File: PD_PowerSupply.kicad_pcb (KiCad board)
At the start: 4 copper layers, 59.3 x 45.5 mm, 75 parts, among them J1 2.54mm Header, J2 Screw Terminal, Q1 STL6P3LLH6, Q2 STL6P3LLH6, U1 LM1117LD-3.3, U2 STUSB4500QTR, U3 LMR16006YQ5, U4 LTM8074IY, U5 LTC7106EDDB-1, U6 LMP92064SDE_NOPB, U7 AQV252GAX, U8 BMD-340-A-R, U9 USB6B1

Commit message: completed routing. Ready for eval.
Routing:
- net /SCLK: track 2.42 -> 57.0 mm, vias 0 -> 3
- net /LTC7106_EN: track 3.65 -> 57.3 mm, vias 0 -> 2
- net /MISO: track 11.0 -> 64.1 mm, vias 1 -> 3
- net /MOSI: track 7.21 -> 58.3 mm, vias 1 -> 3
- net /LTC7106_CSB: track 2.42 -> 50.8 mm, vias 0 -> 2
- net /LMP92064_CSB: track 2.42 -> 34.8 mm, vias 0 -> 2
- net /STUSB_POK3: track 1.18 -> 26.8 mm, vias 1 -> 2
- net /STUSB_RESET: track 5.18 -> 30.6 mm, vias 0 -> 2
- net /STUSB_POK2: track 9.70 -> 34.6 mm, vias 1 -> 2
- net +5V: track 62.8 -> 80.8 mm, vias 0 -> 2
- net /OUTPUT_EN: track 40.2 -> 56.5 mm, vias 0 -> 2
- net +3V3: track 31.1 -> 33.3 mm, vias 12 -> 14
- net GND: track 104.3 -> 102.8 mm, vias 68 -> 78
- net Net-(R1-Pad2): track 34.1 -> 34.6 mm
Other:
- board size 59.3 x 45.5 mm -> 59.3 x 46 mm

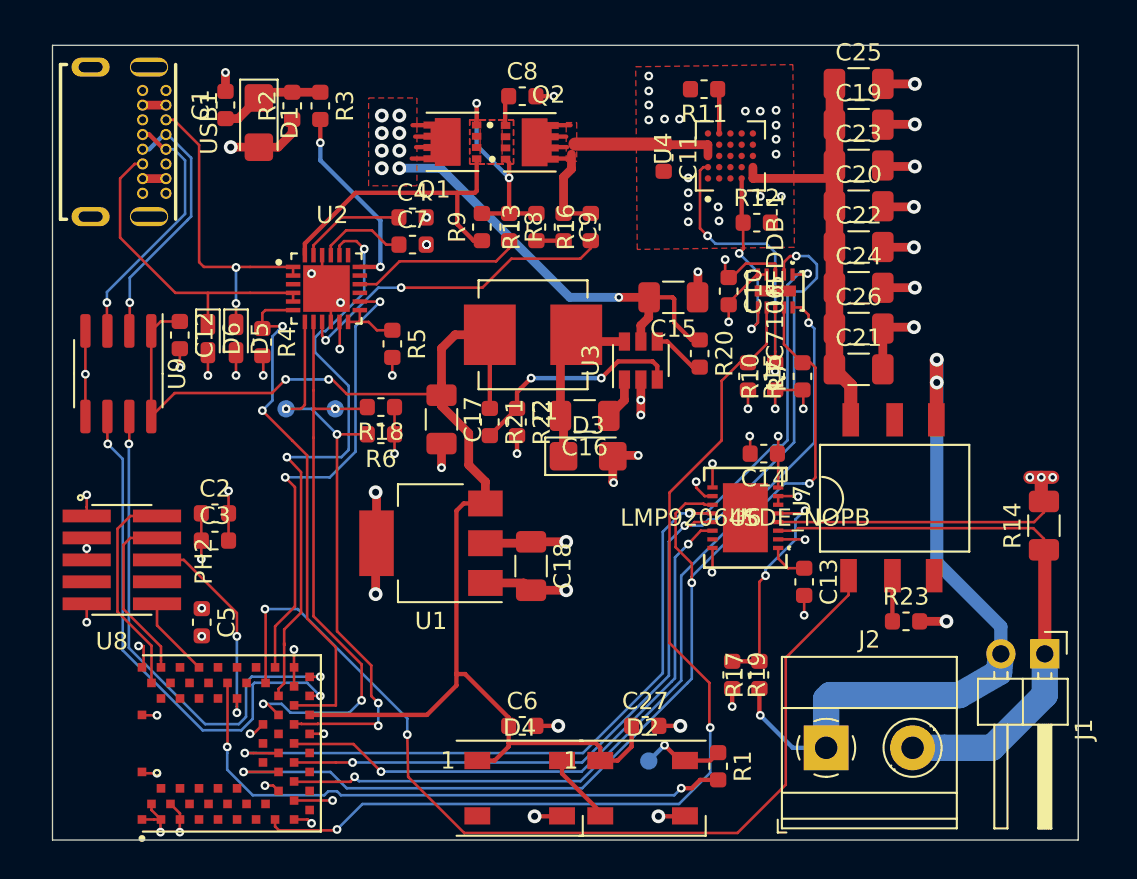
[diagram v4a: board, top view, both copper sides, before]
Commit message: Fixed DRC errors, moved silkscreen
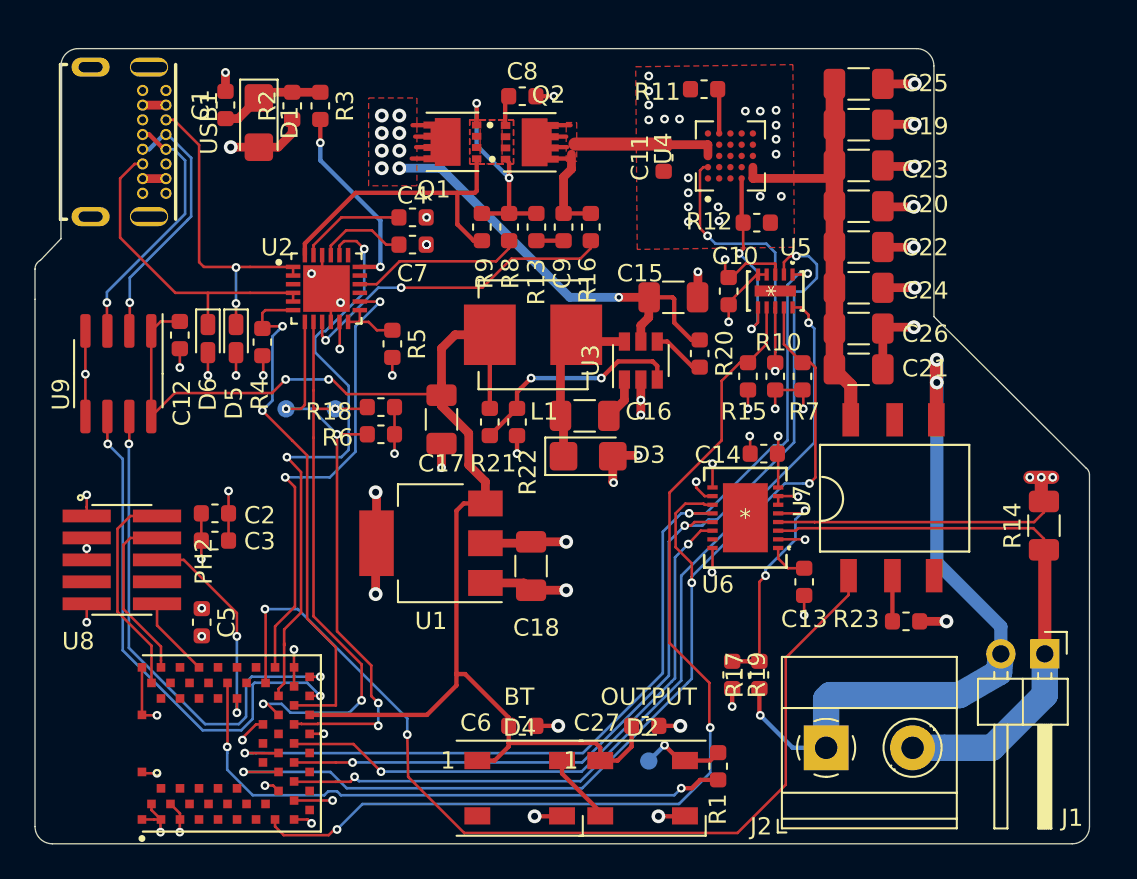
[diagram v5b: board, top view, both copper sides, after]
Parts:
- renumbered TP3 to LED_DATA1
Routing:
- net GND: track 102.8 -> 104.7 mm, vias 78 -> 77
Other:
- board size 59.3 x 46 mm -> 61 x 46 mm
- net class Default: clearance 0.2 -> 0.15
- rule trace_clearance: 0.2 -> 0.15
- board text added: "BT"
- board text added: "OUTPUT"

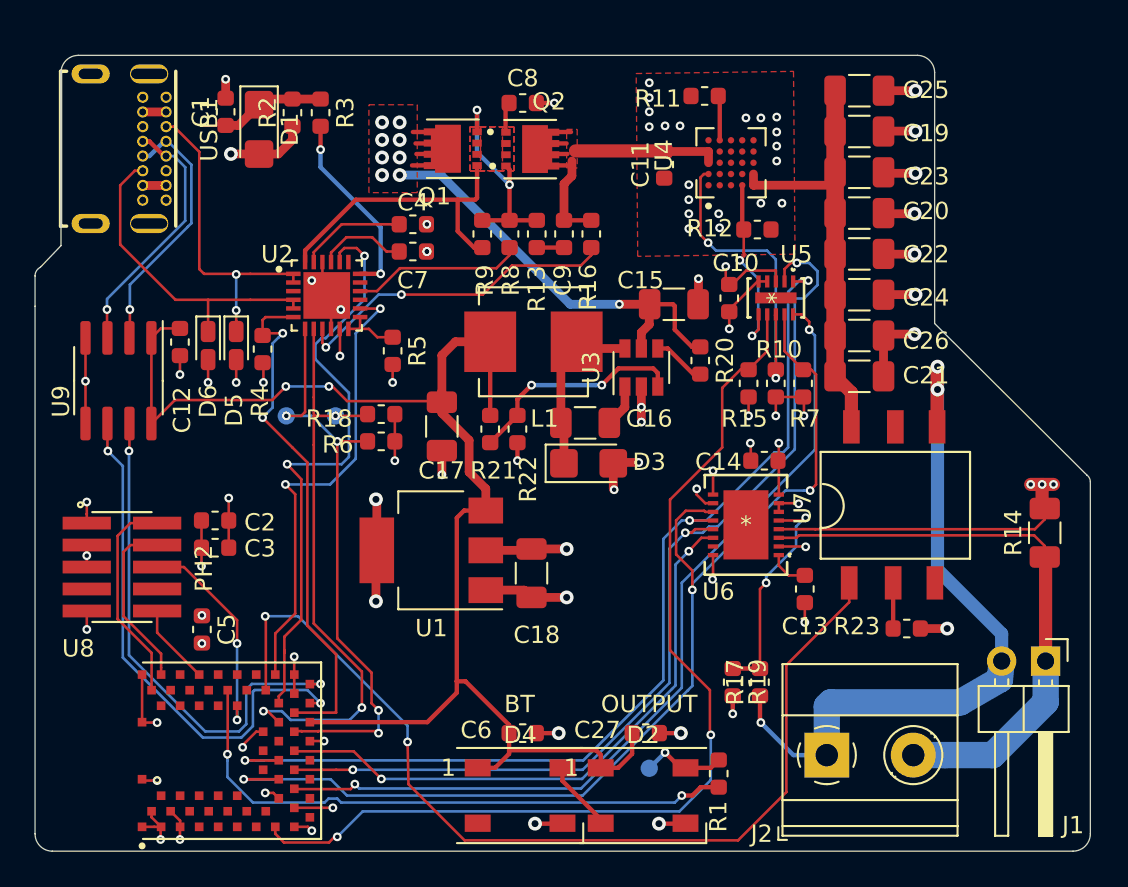
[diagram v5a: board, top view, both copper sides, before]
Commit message: Setup fab drawing and remove designators from silk
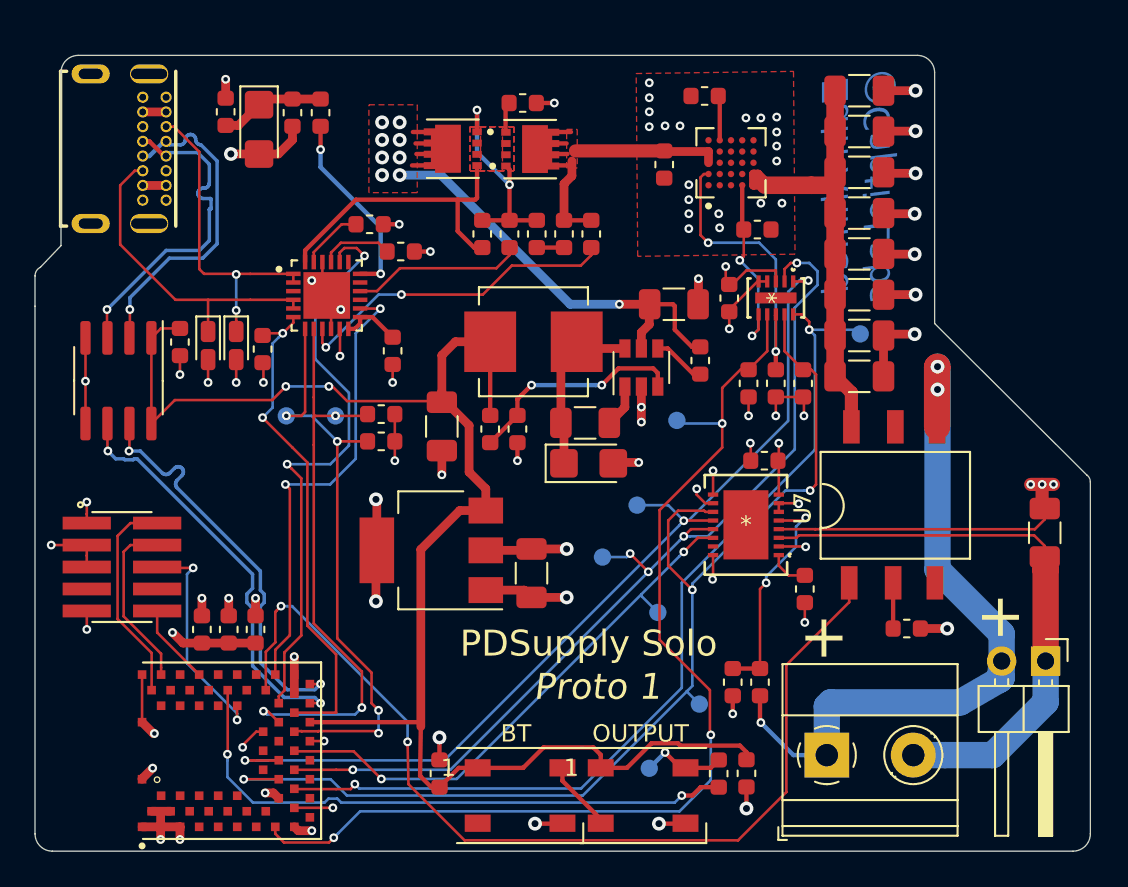
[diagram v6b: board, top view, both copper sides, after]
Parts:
- added LMP_CSB1: TestPoint, TestPoint:TestPoint_Pad_D1.0mm, B.Cu at (148.1, 105.9)
- added LTC_CSB1: TestPoint, TestPoint:TestPoint_Pad_D1.0mm, B.Cu at (159.8, 89.8)
- added LTC_EN1: TestPoint, TestPoint:TestPoint_Pad_D1.0mm, B.Cu at (149.2, 94.8)
- added MISO1: TestPoint, TestPoint:TestPoint_Pad_D1.0mm, B.Cu at (150.5, 111.2)
- added MOSI1: TestPoint, TestPoint:TestPoint_Pad_D1.0mm, B.Cu at (146.9, 99.7)
- added SCLK1: TestPoint, TestPoint:TestPoint_Pad_D1.0mm, B.Cu at (144.9, 102.7)
- moved C2 6.72 mm to (124.8, 106.9), turned to 90 degrees
- moved C27 6.27 mm to (153.2, 115.2), turned to 270 degrees
- moved C6 5.35 mm to (135.5, 115.2), turned to 90 degrees
- moved C3 4.79 mm to (123.3, 106.9), turned to 90 degrees
- moved C4 2.50 mm to (131.4, 83.5)
- moved C7 0.70 mm to (133.2, 85.1)
- turned C5 to 90 degrees
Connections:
- net Net-(U8-Pad67) renamed /USB_TVS_N
- net Net-(U8-Pad68) renamed /USB_TVS_P
- net Net-(U9-Pad2) renamed /USB_D_P
- net Net-(U9-Pad3) renamed /USB_D_N
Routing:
- net +5V: track 80.8 -> 89.1 mm
- net /USB_TVS_N: track 30.5 -> 24.0 mm
- net /USB_TVS_P: track 29.2 -> 23.9 mm
- net /USB_D_N: track 14.8 -> 19.3 mm
- net /USB_D_P: track 15.3 -> 19.4 mm
- net GND: track 104.7 -> 108.3 mm, vias 77 -> 76
- net /LTC7106_EN: track 57.6 -> 61.0 mm, vias 2 -> 3
- net /LTC7106_CSB: track 50.8 -> 53.8 mm
- net /LMP92064_CSB: track 34.8 -> 32.1 mm
- net +3V3: track 33.3 -> 35.7 mm, vias 14 -> 13
- net /MOSI: track 58.3 -> 56.1 mm
- net Net-(C4-Pad1): track 6.18 -> 4.12 mm
- net Net-(R10-Pad2): track 19.4 -> 17.4 mm
- net /MISO: track 64.1 -> 65.8 mm
- net /STUSB_RESET: track 30.6 -> 29.0 mm
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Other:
- board text added: "+"
- board text added: "KEEPOUT"
- board text added: "L1"
- board text added: "PDSupply Solo"
- board text added: "PH2"
- board text added: "Proto 1"
- board text added: "Q1"
- board text added: "Q2"
- board text added: "U2"
- board text added: "U4"
- board text added: "U7"
- board text added: "U8"
- board text added: "USB1"
- board text added: "Zain Ahmed @CaptioLabs"

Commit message: Generated gerbers, started BOM setup for PCBWay
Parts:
- moved R14 2.60 mm to (167.9, 101.3)
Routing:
- net GND: track 108.3 -> 105.3 mm, vias 76 -> 82
- net Net-(J1-Pad1): track 33.0 -> 32.1 mm
- net /vSINK: track 23.1 -> 23.7 mm
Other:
- board text added: "-"
- board text added: "@zainahm3d @CaptioLabs"
- board text removed: "Zain Ahmed @CaptioLabs"

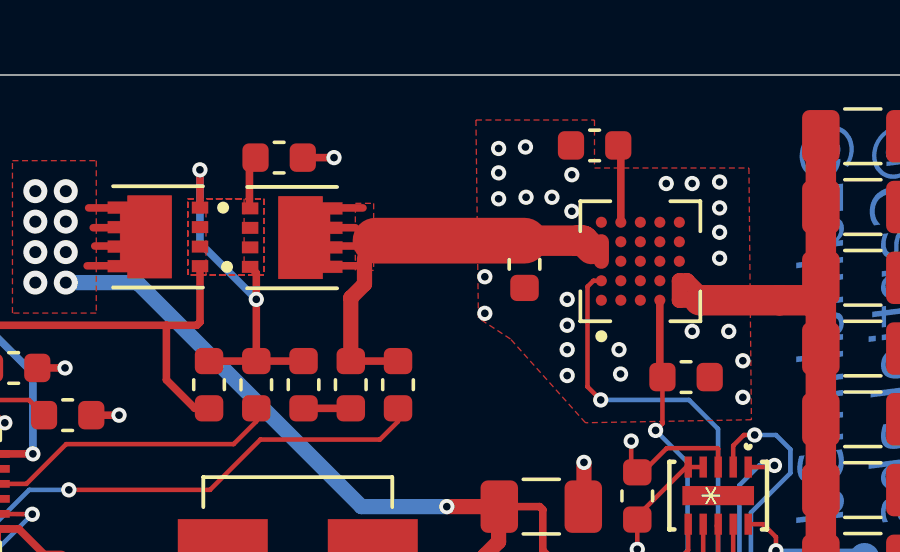
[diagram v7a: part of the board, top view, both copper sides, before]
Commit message: Generate gerbers, drill, centroid, and BOM
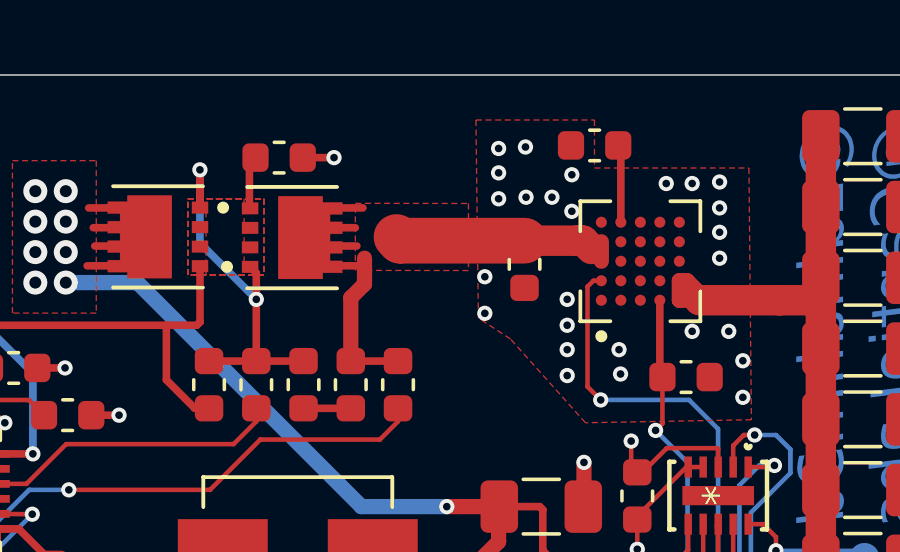
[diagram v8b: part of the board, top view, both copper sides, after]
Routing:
- net /vSINK: track 23.7 -> 22.1 mm
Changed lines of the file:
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@@
   (general
     (thickness 1.6)
-    (drawings 38)
-    (tracks 1058)
+    (drawings 39)
+    (tracks 1057)
     (zones 0)
     (modules 81)
@@
   (layers
     (0 F.Cu signal)
-    (1 In1.Cu power hide)
-    (2 In2.Cu power hide)
+    (1 In1.Cu power)
+    (2 In2.Cu power)
     (31 B.Cu signal)
     (32 B.Adhes user)
@@
   )
   (setup
-    (last_trace_width 1.016)
+    (last_trace_width 0.25)
     (user_trace_width 0.1524)
     (user_trace_width 0.254)
@@
   (module AQV252GAX:SOP6 (layer F.Cu)
     (at 166.1352 99.9072 90)
+    (attr smd)
     (fp_text reference U7 (at -0.000005 -9.674755 90) (layer F.SilkS) hide
       (effects (font (size 1.002354 1.002354) (thickness 0.015)))
@@
   (module BMD-340-A-R:RIGADO_BMD-340-A-R (layer F.Cu)
     (at 121.1264 113.928)
+    (attr smd)
     (fp_text reference U8 (at -6.5376 -5.909865) (layer F.SilkS) hide
       (effects (font (size 1.004228 1.004228) (thickness 0.015)))
@@
   (module LQH66SN220M03L:IND_LQH66SN220M03L (layer F.Cu)
     (at 140.8988 90.288 180)
+    (attr smd)
     (fp_text reference L1 (at -0.635 -4.445) (layer F.SilkS) hide
       (effects (font (size 1 1) (thickness 0.015)))
@@
   (module footprints:LMP92064SDE&slash_NOPB (layer F.Cu)
     (at 153.1812 100.8724 180)
+    (attr smd)
     (fp_text reference U6 (at 1.5924 -3.862) (layer F.SilkS) hide
       (effects (font (size 1 1) (thickness 0.15)))
@@
   (module ul_LTC7106EDDB:LTC7106EDDB (layer F.Cu)
     (at 154.9124 87.755345 270)
+    (attr smd)
     (fp_text reference U5 (at -2.520945 -1.1764 180) (layer F.SilkS) hide
       (effects (font (size 1 1) (thickness 0.15)))
@@
   (module LTM8074IY_PBF:BGA25C65P5X5_400X400X198N (layer F.Cu)
     (at 152.3176 79.9428 90)
+    (attr smd)
     (fp_text reference U4 (at 0.425 -3.885 90) (layer F.SilkS) hide
       (effects (font (size 1 1) (thickness 0.015)))
@@
     (at 117.1132 103.3108 270)
     (descr "translated Allegro footprint")
+    (attr smd)
     (fp_text reference PH2 (at -2.1844 -4.4196 90) (layer F.SilkS) hide
       (effects (font (size 1 1) (thickness 0.015)))
@@
   (module STUSB4500QTR:QFN50P400X400X90-25N (layer F.Cu)
     (at 128.9496 87.6136)
+    (attr smd)
     (fp_text reference U2 (at -2.8608 -2.3792) (layer F.SilkS) hide
       (effects (font (size 1 1) (thickness 0.015)))
@@
   (module STL6P3LLH6:TRANS_STL6P3LLH6 (layer F.Cu)
     (at 140.7098 79.1554)
+    (attr smd)
     (fp_text reference Q2 (at 1.085 -2.755) (layer F.SilkS) hide
       (effects (font (size 1 1) (thickness 0.015)))
@@
   (module STL6P3LLH6:TRANS_STL6P3LLH6 (layer F.Cu)
     (at 136.24 79.13 180)
+    (attr smd)
     (fp_text reference Q1 (at 1.085 -2.755) (layer F.SilkS) hide
       (effects (font (size 1 1) (thickness 0.015)))
@@
       (net 17 "Net-(C8-Pad1)"))
   )
-  (dimension 46 (width 0.065) (layer F.SilkS)
-    (gr_text "46.000 mm" (at 106.5738 96.7344 90) (layer F.SilkS)
+  (target plus (at 107.7888 122.9344) (size 5) (width 0.05) (layer Edge.Cuts))
+  (dimension 46 (width 0.065) (layer Dwgs.User)
+    (gr_text "46.000 mm" (at 106.5738 96.7344 90) (layer Dwgs.User)
       (effects (font (size 1 1) (thickness 0.15)))
     )
@@
     (arrow2b (pts (xy 107.7888 119.7344) (xy 107.202379 118.607896)))
   )
-  (dimension 61.2 (width 0.065) (layer F.SilkS)
-    (gr_text "61.200 mm" (at 142.5888 124.149399) (layer F.SilkS)
+  (dimension 61.2 (width 0.065) (layer Dwgs.User)
+    (gr_text "61.200 mm" (at 142.5888 124.149399) (layer Dwgs.User)
       (effects (font (size 1 1) (thickness 0.15)))
     )
@@
   (gr_line (start 112.0888 118.7344) (end 112.0888 88.2344) (layer Edge.Cuts) (width 0.05))
   (gr_circle (center 119.1452 115.6044) (end 119.196 115.7568) (layer F.SilkS) (width 0.065))
-  (via (at 150.034 78.2784) (size 0.508) (drill 0.254) (layers F.Cu B.Cu) (net 3))
-  (via (at 150.034 77.0592) (size 0.508) (drill 0.254) (layers F.Cu B.Cu) (net 3))
-  (via (at 147.134 81.6784) (size 0.508) (drill 0.254) (layers F.Cu B.Cu) (net 3))
-  (via (at 147.134 80.4592) (size 0.508) (drill 0.254) (layers F.Cu B.Cu) (net 3))
-  (via (at 155.734 84.4784) (size 0.508) (drill 0.254) (layers F.Cu B.Cu) (net 3))
-  (via (at 155.734 83.2592) (size 0.508) (drill 0.254) (layers F.Cu B.Cu) (net 3))
   (segment (start 129.5592 96.148) (end 129.5592 96.148) (width 0.1524) (layer B.Cu) (net 1))
   (segment (start 128.086 94.5732) (end 129.5592 96.0464) (width 0.1524) (layer B.Cu) (net 1))
@@
   (segment (start 125.4844 111.8344) (end 130.586 111.8344) (width 0.1524) (layer B.Cu) (net 2))
   (segment (start 125.292 111.642) (end 125.4844 111.8344) (width 0.1524) (layer B.Cu) (net 2))
+  (via (at 150.034 78.2784) (size 0.508) (drill 0.254) (layers F.Cu B.Cu) (net 3))
+  (via (at 150.034 77.0592) (size 0.508) (drill 0.254) (layers F.Cu B.Cu) (net 3))
+  (via (at 147.134 81.6784) (size 0.508) (drill 0.254) (layers F.Cu B.Cu) (net 3))
+  (via (at 147.134 80.4592) (size 0.508) (drill 0.254) (layers F.Cu B.Cu) (net 3))
+  (via (at 155.734 84.4784) (size 0.508) (drill 0.254) (layers F.Cu B.Cu) (net 3))
+  (via (at 155.734 83.2592) (size 0.508) (drill 0.254) (layers F.Cu B.Cu) (net 3))
   (via (at 124.8348 105.1142) (size 0.508) (drill 0.254) (layers F.Cu B.Cu) (net 3))
   (via (at 123.2854 105.1142) (size 0.508) (drill 0.254) (layers F.Cu B.Cu) (net 3))
@@
   (segment (start 142.6656 81.162) (end 143.1228 80.7048) (width 0.508) (layer F.Cu) (net 8))
   (segment (start 143.1228 80.7048) (end 143.1228 79.8412) (width 0.508) (layer F.Cu) (net 8))
-  (segment (start 143.6888 79.2569) (end 143.6888 78.8344) (width 0.254) (layer F.Cu) (net 8))
-  (segment (start 143.6888 79.2569) (end 143.6888 78.7344) (width 0.254) (layer F.Cu) (net 8))
   (segment (start 141.9804 78.1648) (end 143.072 78.1648) (width 0.254) (layer F.Cu) (net 8))
   (segment (start 140.9898 79.1554) (end 141.9804 78.1648) (width 0.254) (layer F.Cu) (net 8))
-  (segment (start 148.4568 79.2569) (end 143.4888 79.2569) (width 1.524) (layer F.Cu) (net 8))
   (segment (start 148.4568 79.2569) (end 150.2113 79.2569) (width 1.016) (layer F.Cu) (net 8))
   (segment (start 150.4113 79.2569) (end 150.6888 79.5344) (width 1.016) (layer F.Cu) (net 8))
   (segment (start 150.2113 79.2569) (end 150.4113 79.2569) (width 1.016) (layer F.Cu) (net 8))
+  (segment (start 144.3113 79.2569) (end 144.1888 79.1344) (width 1.524) (layer F.Cu) (net 8))
+  (segment (start 148.4568 79.2569) (end 144.3113 79.2569) (width 1.524) (layer F.Cu) (net 8))
   (via (at 156.534 94.5732) (size 0.508) (drill 0.254) (layers F.Cu B.Cu) (net 9))
   (via (at 154.9084 94.5732) (size 0.508) (drill 0.254) (layers F.Cu B.Cu) (net 9))
@@
   (segment (start 144.49079 92.7952) (end 140.786 92.7952) (width 0.254) (layer B.Cu) (net 58))
   (segment (start 144.85 92.7952) (end 144.49079 92.7952) (width 0.254) (layer B.Cu) (net 58))
-  (segment (start 148.086 92.0952) (end 147.8208 91.83) (width 0.254) (layer F.Cu) (net 58))
-  (segment (start 148.086 92.8792) (end 148.086 92.0952) (width 0.254) (layer F.Cu) (net 58))
+  (segment (start 147.8208 91.83) (end 145.8152 91.83) (width 0.254) (layer F.Cu) (net 58) (status 1000000))
+  (segment (start 148.086 92.8792) (end 148.086 92.0952) (width 0.254) (layer F.Cu) (net 58) (status 1000000))
+  (segment (start 148.086 92.0952) (end 147.8208 91.83) (width 0.254) (layer F.Cu) (net 58) (status 1000000))
   (segment (start 145.8152 91.83) (end 144.85 92.7952) (width 0.254) (layer F.Cu) (net 58))
-  (segment (start 147.8208 91.83) (end 145.8152 91.83) (width 0.254) (layer F.Cu) (net 58))
   (segment (start 153.6176 81.2428) (end 153.6176 80.5928) (width 0.508) (layer F.Cu) (net 59))
   (segment (start 158.3344 75.7772) (end 158.3344 92.0556) (width 1.016) (layer F.Cu) (net 59))
@@
     (polygon
       (pts
-        (xy 143.4276 80.248178) (xy 142.818 80.2476) (xy 142.818 78.0124) (xy 143.4276 78.012978)
+        (xy 146.5888 80.252) (xy 142.818 80.2476) (xy 142.818 78.0124) (xy 146.5888 78.0168)
       )
     )
